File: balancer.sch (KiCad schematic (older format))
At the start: 19 parts, among them J3 AVR-ISP-6, J4 Screw_Terminal_01x03, Q1 IRLZ34N, U1 EL817, U2 ATtiny85-20PU

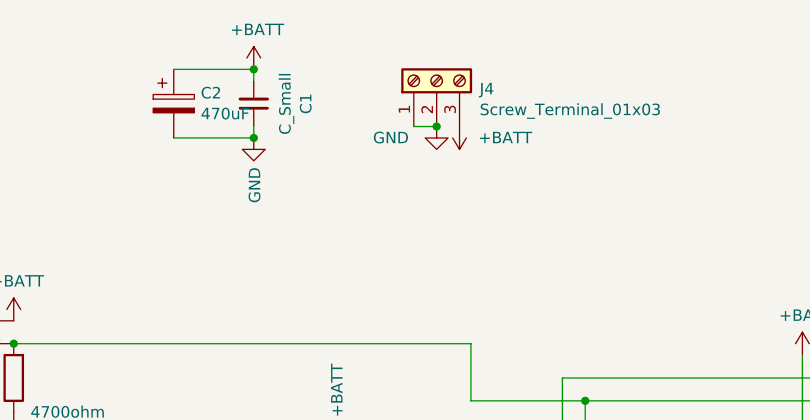
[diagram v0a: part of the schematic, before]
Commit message: changed VBATT connector from 2 GND to 2 VBATT
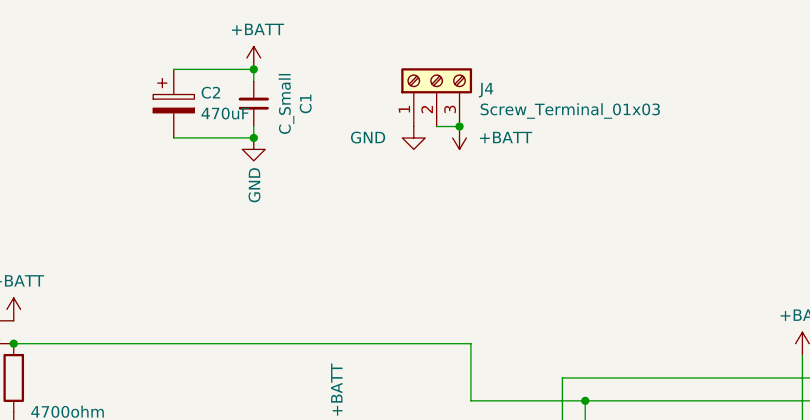
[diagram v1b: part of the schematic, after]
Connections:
- net +BATT: now also J4.2 (Pin_2)
- net GND: no longer J4.2 (Pin_2)
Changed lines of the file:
@@
 L power:GND #PWR05
 U 1 1 62E59AA5
-P 4150 1000
-F 0 "#PWR05" H 4150 750 50  0001 C CNN
-F 1 "GND" H 3950 950 50  0000 C CNN
-F 2 "" H 4150 1000 50  0001 C CNN
-F 3 "" H 4150 1000 50  0001 C CNN
-	1    4150 1000
+P 4050 1000
+F 0 "#PWR05" H 4050 750 50  0001 C CNN
+F 1 "GND" H 3850 950 50  0000 C CNN
+F 2 "" H 4050 1000 50  0001 C CNN
+F 3 "" H 4050 1000 50  0001 C CNN
+	1    4050 1000
 	1    0    0    -1
 $EndComp
@@
 Connection ~ 3350 1050
 Connection ~ 3350 750
-Wire Wire Line
-	4050 1000 4150 1000
-Connection ~ 4150 1000
 $Comp
 L Device:CP C3
@@
 Wire Wire Line
 	7200 2350 7300 2350
+Wire Wire Line
+	4150 1000 4250 1000
+Connection ~ 4250 1000
 $EndSCHEMATC

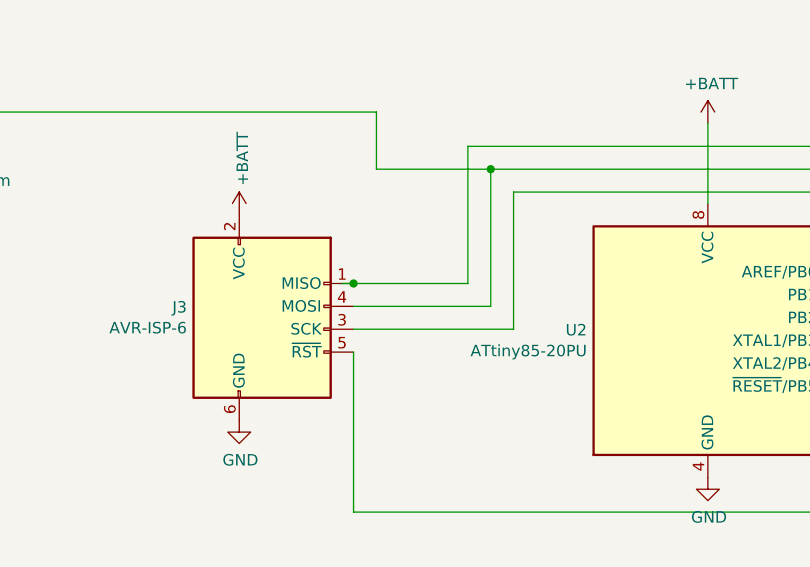
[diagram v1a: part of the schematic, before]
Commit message: removed junction in schema
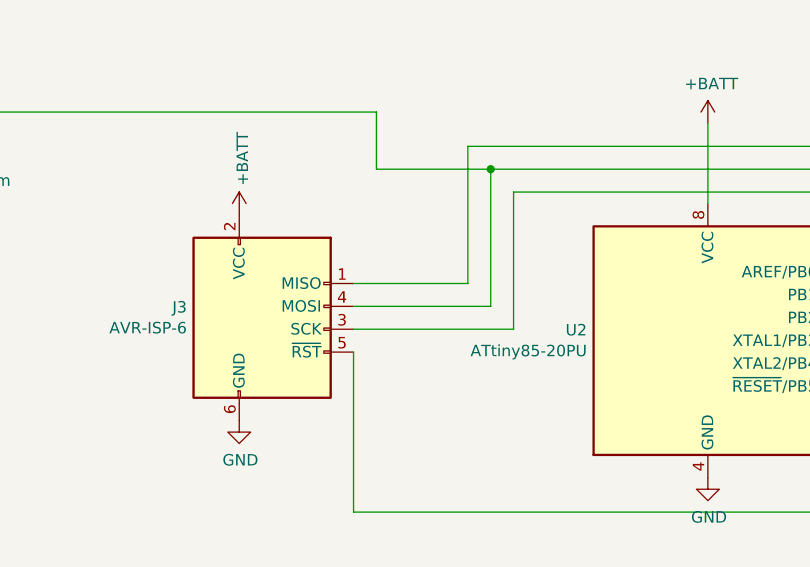
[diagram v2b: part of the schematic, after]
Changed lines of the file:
@@
 	6450 2300 6450 2850
 Wire Wire Line
-	4150 2700 4200 2700
-Wire Wire Line
 	4700 2700 4700 2100
-Connection ~ 4200 2700
 Wire Wire Line
 	4800 2800 4800 2200
@@
 	4200 2800 4800 2800
 Wire Wire Line
-	4200 2700 4700 2700
-Wire Wire Line
 	4800 2200 4300 2200
 Connection ~ 4800 2200
@@
 	4150 1000 4250 1000
 Connection ~ 4250 1000
+Wire Wire Line
+	4700 2700 4200 2700
 $EndSCHEMATC
